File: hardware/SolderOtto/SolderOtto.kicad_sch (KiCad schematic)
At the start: 0 parts

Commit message: save wip
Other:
- added sheet overview (untitled.kicad_sch)
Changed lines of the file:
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@@
+	)
+	(sheet
+		(at 223.52 80.645)
+		(size 32.385 22.225)
+		(fields_autoplaced yes)
+		(stroke
+			(width 0.1524)
+			(type solid)
+		)
+		(fill
+			(color 255 255 194 1.0000)
+		)
+		(property "Sheetname" "overview"
+			(at 223.52 79.9334 0)
+			(effects
+				(font
+					(size 1.27 1.27)
+				)
+				(justify left bottom)
+			)
+		)
+		(property "Sheetfile" "untitled.kicad_sch"
+			(at 223.52 103.4546 0)
+			(effects
+				(font
+					(size 1.27 1.27)
+				)
+				(justify left top)
+			)
+		)
+		(instances
+			(project "SolderOtto"
+				(path "/04e99464-bf33-4a4f-8397-d26b5ec904f3"
+					(page "9")
+				)
+			)
+		)
 	)
 	(sheet

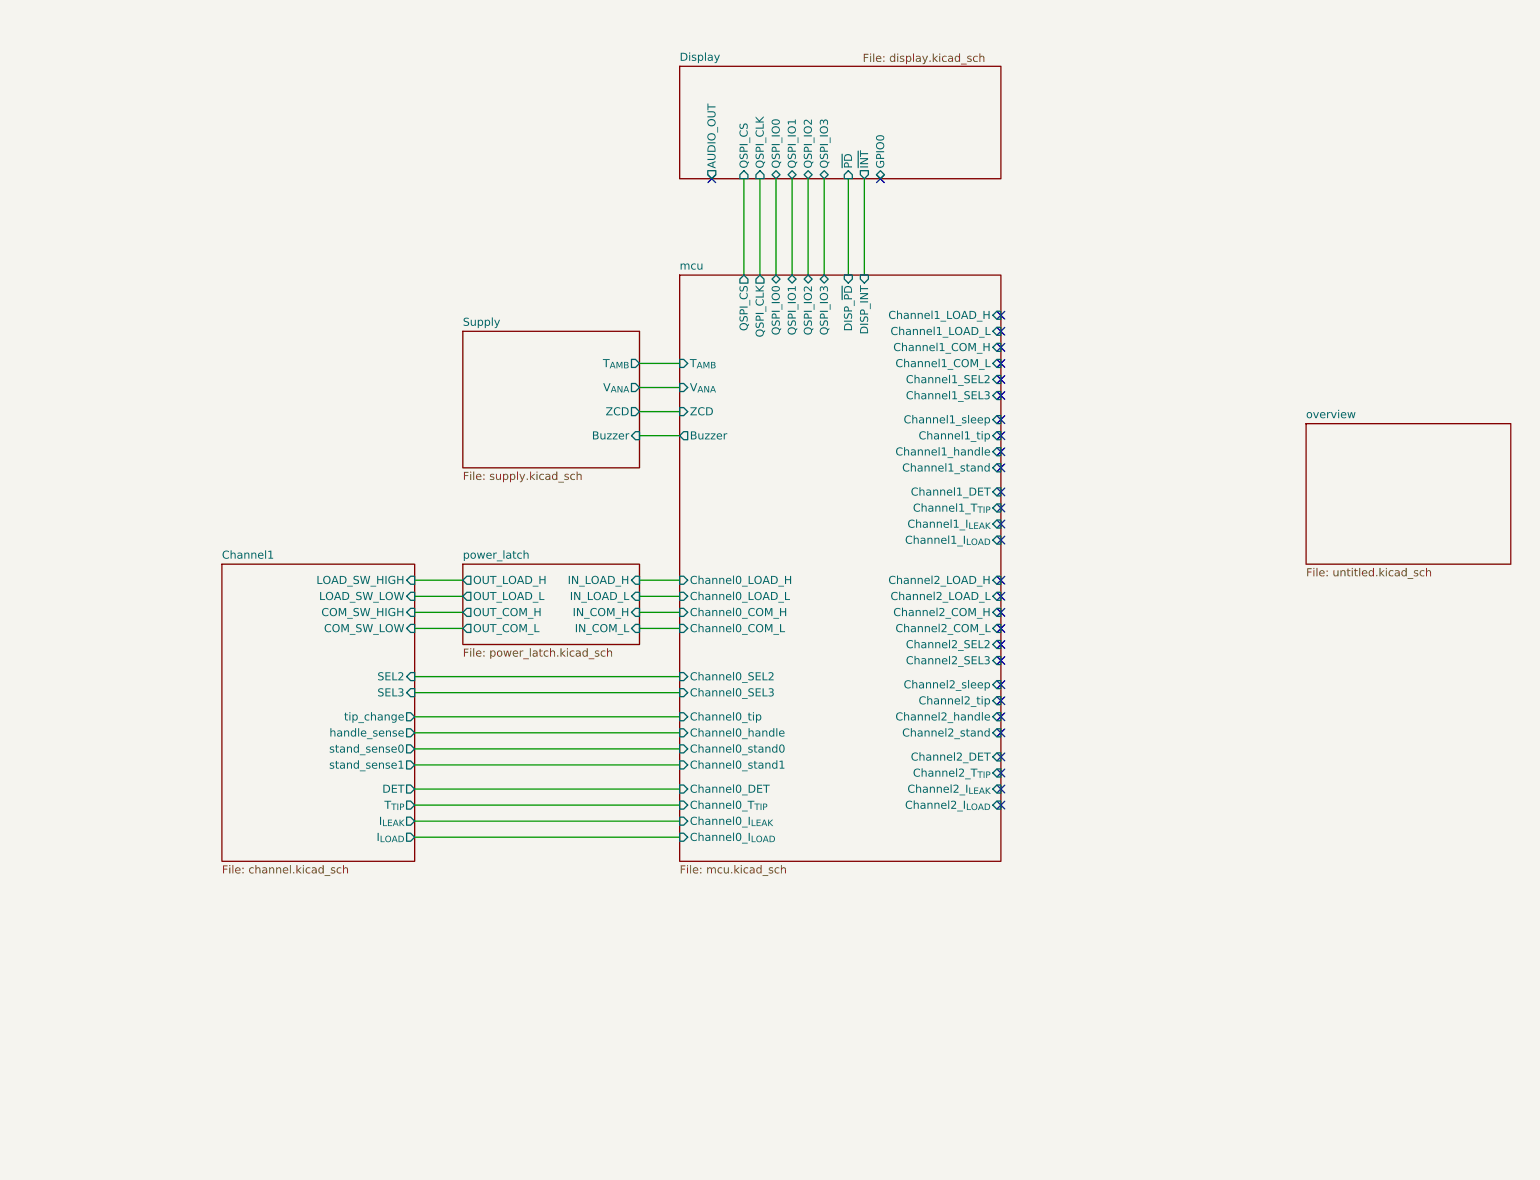
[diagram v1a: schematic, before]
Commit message: add support for tweezers AM-120
change mcu to stm32h573VI
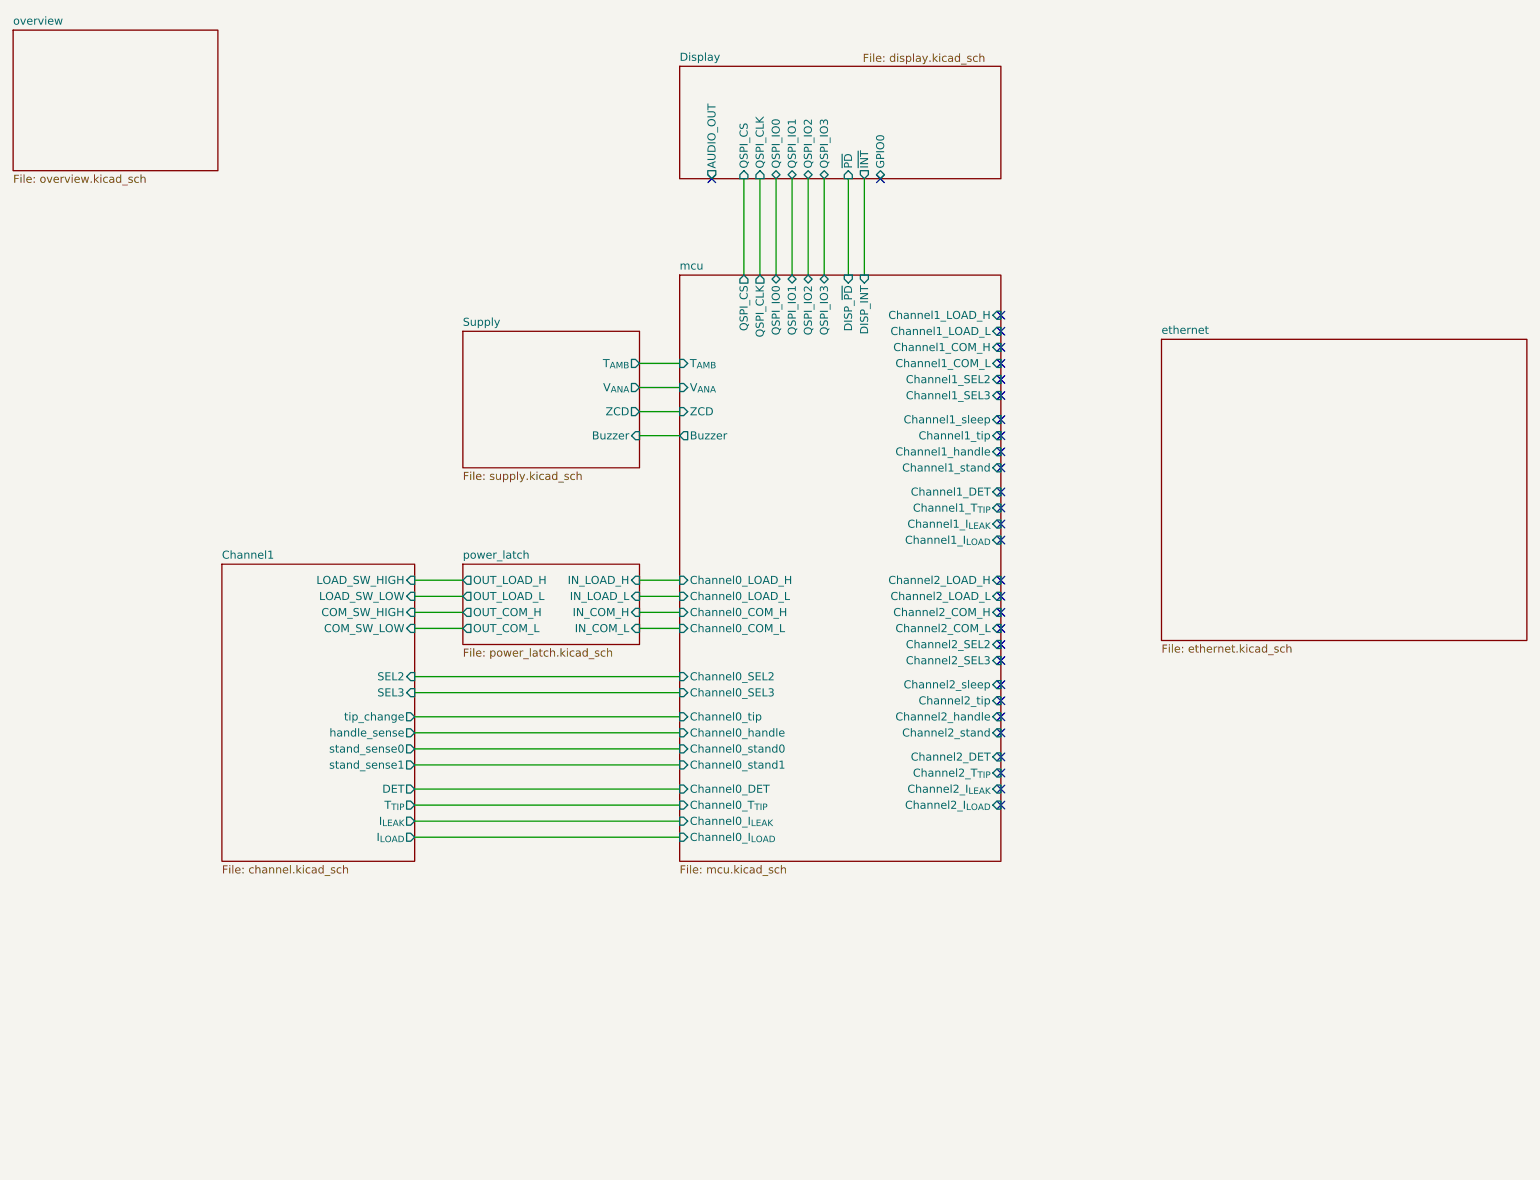
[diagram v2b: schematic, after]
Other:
- added sheet ethernet (ethernet.kicad_sch)
- sheet overview: file untitled.kicad_sch -> overview.kicad_sch
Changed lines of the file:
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@@
 			(project "SolderOtto"
 				(path "/04e99464-bf33-4a4f-8397-d26b5ec904f3"
-					(page "5")
+					(page "6")
 				)
 			)
@@
 			(project "SolderOtto"
 				(path "/04e99464-bf33-4a4f-8397-d26b5ec904f3"
-					(page "2")
+					(page "3")
+				)
+			)
+		)
+	)
+	(sheet
+		(at 200.66 67.31)
+		(size 57.785 47.625)
+		(fields_autoplaced yes)
+		(stroke
+			(width 0.1524)
+			(type solid)
+		)
+		(fill
+			(color 255 255 194 1.0000)
+		)
+		(property "Sheetname" "ethernet"
+			(at 200.66 66.5984 0)
+			(effects
+				(font
+					(size 1.27 1.27)
+				)
+				(justify left bottom)
+			)
+		)
+		(property "Sheetfile" "ethernet.kicad_sch"
+			(at 200.66 115.5196 0)
+			(effects
+				(font
+					(size 1.27 1.27)
+				)
+				(justify left top)
+			)
+		)
+		(instances
+			(project "SolderOtto"
+				(path "/04e99464-bf33-4a4f-8397-d26b5ec904f3"
+					(page "16")
 				)
 			)
@@
 			(project "SolderOtto"
 				(path "/04e99464-bf33-4a4f-8397-d26b5ec904f3"
-					(page "6")
+					(page "7")
 				)
 			)
@@
 			(project "SolderOtto"
 				(path "/04e99464-bf33-4a4f-8397-d26b5ec904f3"
-					(page "3")
+					(page "4")
 				)
 			)
@@
 	)
 	(sheet
-		(at 223.52 80.645)
+		(at 19.05 18.415)
 		(size 32.385 22.225)
 		(fields_autoplaced yes)
@@
 		)
 		(property "Sheetname" "overview"
-			(at 223.52 79.9334 0)
+			(at 19.05 17.7034 0)
 			(effects
 				(font
@@
 			)
 		)
-		(property "Sheetfile" "untitled.kicad_sch"
-			(at 223.52 103.4546 0)
+		(property "Sheetfile" "overview.kicad_sch"
+			(at 19.05 41.2246 0)
 			(effects
 				(font
@@
 			(project "SolderOtto"
 				(path "/04e99464-bf33-4a4f-8397-d26b5ec904f3"
-					(page "9")
+					(page "2")
 				)
 			)
@@
 			(project "SolderOtto"
 				(path "/04e99464-bf33-4a4f-8397-d26b5ec904f3"
-					(page "4")
-				)
-			)
+					(page "5")
+				)
+			)

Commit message: save wip
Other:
- removed sheet power_latch
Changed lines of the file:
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@@
-	)
-	(sheet
-		(at 90.17 102.87)
-		(size 27.94 12.7)
-		(fields_autoplaced yes)
-		(stroke
-			(width 0.1524)
-			(type solid)
-		)
-		(fill
-			(color 255 255 194 1.0000)
-		)
-		(property "Sheetname" "power_latch"
-			(at 90.17 102.1584 0)
-			(effects
-				(font
-					(size 1.27 1.27)
-				)
-				(justify left bottom)
-			)
-		)
-		(property "Sheetfile" "power_latch.kicad_sch"
-			(at 90.17 116.1546 0)
-			(effects
-				(font
-					(size 1.27 1.27)
-				)
-				(justify left top)
-			)
-		)
-		(pin "IN_LOAD_L" input
-			(at 118.11 107.95 0)
-			(effects
-				(font
-					(size 1.27 1.27)
-				)
-				(justify right)
-			)
-		)
-		(pin "IN_LOAD_H" input
-			(at 118.11 105.41 0)
-			(effects
-				(font
-					(size 1.27 1.27)
-				)
-				(justify right)
-			)
-		)
-		(pin "IN_COM_L" input
-			(at 118.11 113.03 0)
-			(effects
-				(font
-					(size 1.27 1.27)
-				)
-				(justify right)
-			)
-		)
-		(pin "IN_COM_H" input
-			(at 118.11 110.49 0)
-			(effects
-				(font
-					(size 1.27 1.27)
-				)
-				(justify right)
-			)
-		)
-		(pin "OUT_LOAD_H" output
-			(at 90.17 105.41 180)
-			(effects
-				(font
-					(size 1.27 1.27)
-				)
-				(justify left)
-			)
-		)
-		(pin "OUT_COM_H" output
-			(at 90.17 110.49 180)
-			(effects
-				(font
-					(size 1.27 1.27)
-				)
-				(justify left)
-			)
-		)
-		(pin "OUT_LOAD_L" output
-			(at 90.17 107.95 180)
-			(effects
-				(font
-					(size 1.27 1.27)
-				)
-				(justify left)
-			)
-		)
-		(pin "OUT_COM_L" output
-			(at 90.17 113.03 180)
-			(effects
-				(font
-					(size 1.27 1.27)
-				)
-				(justify left)
-			)
-		)
-		(instances
-			(project "SolderOtto"
-				(path "/04e99464-bf33-4a4f-8397-d26b5ec904f3"
-					(page "6")
-				)
-			)
-		)
 	)
 	(sheet
@@
 			(project "SolderOtto"
 				(path "/04e99464-bf33-4a4f-8397-d26b5ec904f3"
-					(page "7")
-				)
-			)
+					(page "6")
+				)
+			)

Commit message: wip
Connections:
- no-connect marks 30 -> 2
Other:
- removed sheet ethernet
- removed sheet overview
- sheet Channel1 ports: added COM_SW, LOAD0_SW, LOAD1_SW, LOW_SIDE_SW, SEL1, handle_id, iron_sense, stand_sense; removed COM_SW_HIGH, COM_SW_LOW, LOAD_SW_HIGH, LOAD_SW_LOW, handle_sense, stand_sense0, stand_sense1
- sheet mcu ports: added AAAAAAAA, Channel0_COM_SW, Channel0_LOAD0_SW, Channel0_LOAD1_SW, Channel0_LOW_SIDE_SW, Channel0_SEL1, Channel0_iron, Channel0_stand; removed Channel0_COM_H, Channel0_COM_L, Channel0_LOAD_H, Channel0_LOAD_L, Channel0_stand0, Channel0_stand1, QSPI_CS

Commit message: save wip
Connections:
- no-connect marks 2 -> 4
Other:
- added sheet Channel0 (channel.kicad_sch)
- added sheet Channel2 (channel.kicad_sch)
- added sheet Channel3 (channel.kicad_sch)
- added sheet External connection (external.kicad_sch)
- sheet Display ports: added SPI_MISO, SPI_MOSI; removed QSPI_IO0, QSPI_IO1
- sheet mcu ports: added Channel1_COM_SW, Channel1_LOAD0_SW, Channel1_LOAD1_SW, Channel1_LOW_SIDE_SW, Channel1_SEL1, Channel1_iron, Channel2_COM_SW, Channel2_LOAD0_SW, Channel2_LOAD1_SW, Channel2_LOW_SIDE_SW, Channel2_SEL1, Channel2_iron, Channel3_COM_SW, Channel3_DET, Channel3_I_{LEAK}, Channel3_I_{LOAD}, Channel3_LOAD0_SW, Channel3_LOAD1_SW, Channel3_LOW_SIDE_SW, Channel3_SEL1, Channel3_SEL2, Channel3_SEL3, Channel3_T_{TIP}, Channel3_handle, Channel3_iron, Channel3_stand, Channel3_tip, DISP_CLK, DISP_MISO, DISP_MOSI, DISP_NSS, EXT_0, EXT_1, EXT_2, EXT_3, EXT_4, EXT_5; removed AAAAAAAA, Channel1_COM_H, Channel1_COM_L, Channel1_LOAD_H, Channel1_LOAD_L, Channel1_sleep, Channel2_COM_H, Channel2_COM_L, Channel2_LOAD_H, Channel2_LOAD_L, Channel2_sleep, QSPI_CLK, QSPI_IO0, QSPI_IO1, QSPI_IO2, QSPI_IO3

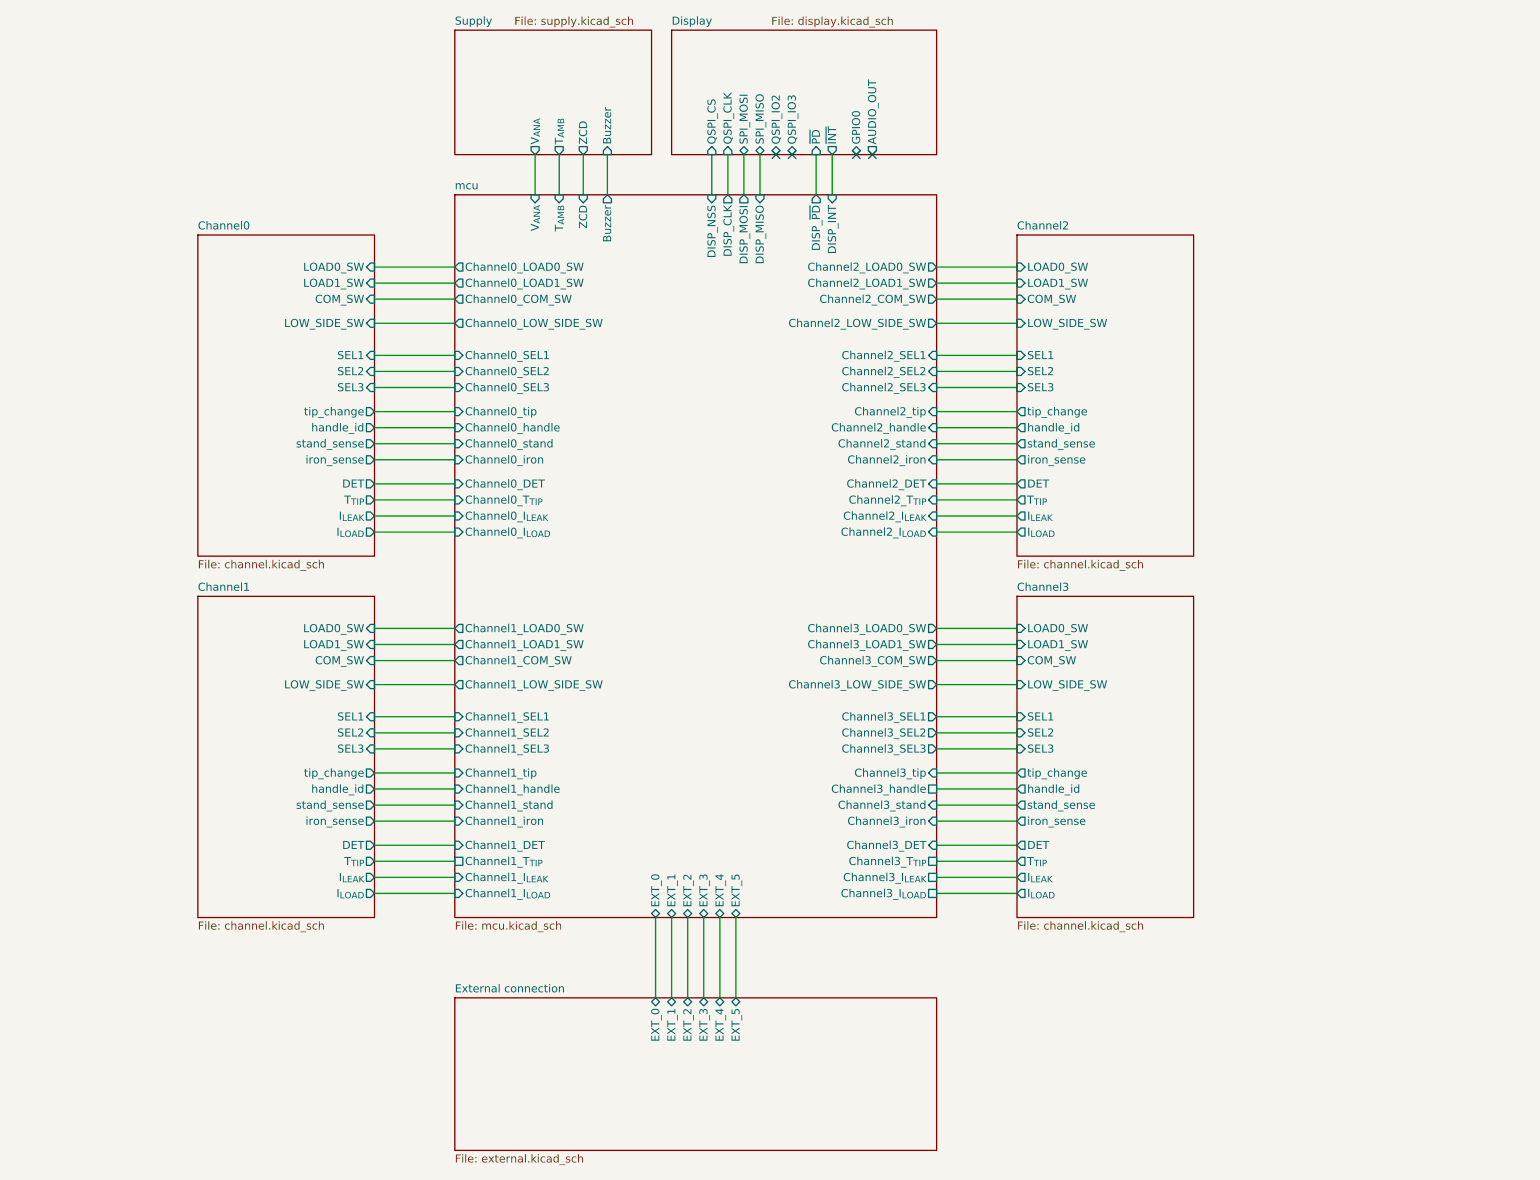
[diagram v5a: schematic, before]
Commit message: update schematic
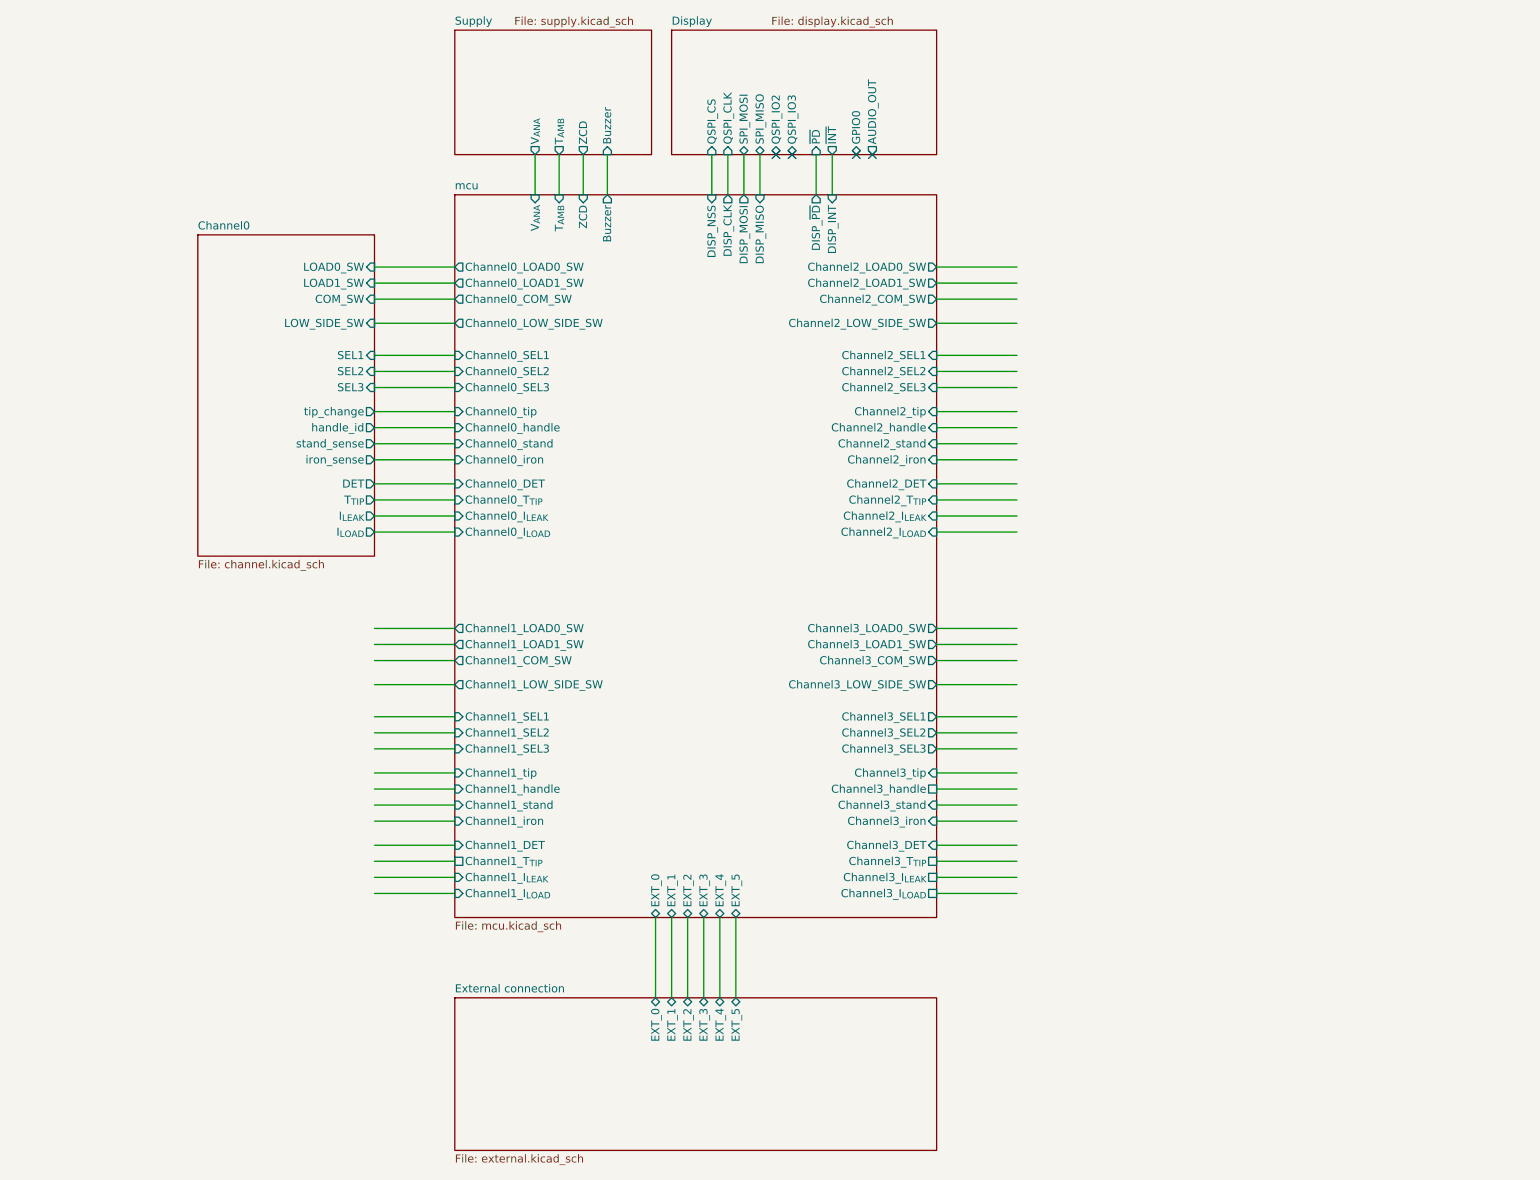
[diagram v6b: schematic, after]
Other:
- removed sheet Channel1
- removed sheet Channel2
- removed sheet Channel3
